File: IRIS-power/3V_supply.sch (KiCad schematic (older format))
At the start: 3 parts

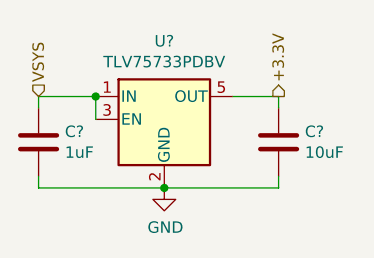
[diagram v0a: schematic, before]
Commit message: Finalized power board V2 schematic, preparing to layout
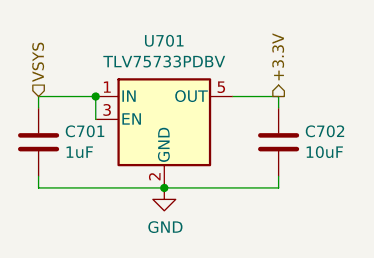
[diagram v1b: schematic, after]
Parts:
- C701, C702: renamed from C?; footprint (none) -> Capacitor_SMD:C_0603_1608Metric
- gave numbers to parts that had none: 1
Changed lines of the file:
@@
 $Descr A4 11693 8268
 encoding utf-8
-Sheet 2 9
+Sheet 7 8
 Title ""
 Date ""
@@
 	5650 3900 5650 3800
 $Comp
-L power:GND #PWR?
+L power:GND #PWR0701
 U 1 1 5F36182F
 P 5950 4200
-F 0 "#PWR?" H 5950 3950 50  0001 C CNN
+F 0 "#PWR0701" H 5950 3950 50  0001 C CNN
 F 1 "GND" H 5955 4027 50  0000 C CNN
 F 2 "" H 5950 4200 50  0001 C CNN
@@
 	6450 3850 6450 3800
 $Comp
-L Device:C C?
+L Device:C C702
 U 1 1 5F36183D
 P 6450 4000
-F 0 "C?" H 6565 4046 50  0000 L CNN
+F 0 "C702" H 6565 4046 50  0000 L CNN
 F 1 "10uF" H 6565 3955 50  0000 L CNN
-F 2 "" H 6488 3850 50  0001 C CNN
+F 2 "Capacitor_SMD:C_0603_1608Metric" H 6488 3850 50  0001 C CNN
 F 3 "~" H 6450 4000 50  0001 C CNN
 	1    6450 4000
@@
 $EndComp
 $Comp
-L Device:C C?
+L Device:C C701
 U 1 1 5F361843
 P 5400 4000
-F 0 "C?" H 5515 4046 50  0000 L CNN
+F 0 "C701" H 5515 4046 50  0000 L CNN
 F 1 "1uF" H 5515 3955 50  0000 L CNN
-F 2 "" H 5438 3850 50  0001 C CNN
+F 2 "Capacitor_SMD:C_0603_1608Metric" H 5438 3850 50  0001 C CNN
 F 3 "~" H 5400 4000 50  0001 C CNN
 	1    5400 4000
@@
 Connection ~ 5650 3800
 $Comp
-L Regulator_Linear:TLV75733PDBV U?
+L Regulator_Linear:TLV75733PDBV U701
 U 1 1 5F36184A
 P 5950 3900
-F 0 "U?" H 5950 4242 50  0000 C CNN
+F 0 "U701" H 5950 4242 50  0000 C CNN
 F 1 "TLV75733PDBV" H 5950 4151 50  0000 C CNN
 F 2 "Package_TO_SOT_SMD:SOT-23-5" H 5950 4225 50  0001 C CIN

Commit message: Finished initial layout without gnd plane
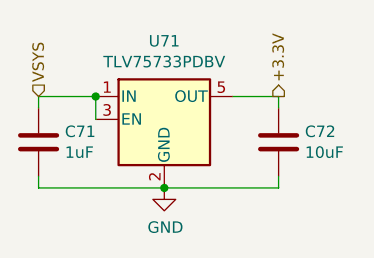
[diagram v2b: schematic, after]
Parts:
- renumbered C701 to C71, C702 to C72, U701 to U71
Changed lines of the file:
@@
 	5650 3900 5650 3800
 $Comp
-L power:GND #PWR0701
+L power:GND #PWR0103
 U 1 1 5F36182F
 P 5950 4200
-F 0 "#PWR0701" H 5950 3950 50  0001 C CNN
+F 0 "#PWR0103" H 5950 3950 50  0001 C CNN
 F 1 "GND" H 5955 4027 50  0000 C CNN
 F 2 "" H 5950 4200 50  0001 C CNN
@@
 	6450 3850 6450 3800
 $Comp
-L Device:C C702
+L Device:C C72
 U 1 1 5F36183D
 P 6450 4000
-F 0 "C702" H 6565 4046 50  0000 L CNN
+F 0 "C72" H 6565 4046 50  0000 L CNN
 F 1 "10uF" H 6565 3955 50  0000 L CNN
 F 2 "Capacitor_SMD:C_0603_1608Metric" H 6488 3850 50  0001 C CNN
@@
 $EndComp
 $Comp
-L Device:C C701
+L Device:C C71
 U 1 1 5F361843
 P 5400 4000
-F 0 "C701" H 5515 4046 50  0000 L CNN
+F 0 "C71" H 5515 4046 50  0000 L CNN
 F 1 "1uF" H 5515 3955 50  0000 L CNN
 F 2 "Capacitor_SMD:C_0603_1608Metric" H 5438 3850 50  0001 C CNN
@@
 Connection ~ 5650 3800
 $Comp
-L Regulator_Linear:TLV75733PDBV U701
+L Regulator_Linear:TLV75733PDBV U71
 U 1 1 5F36184A
 P 5950 3900
-F 0 "U701" H 5950 4242 50  0000 C CNN
+F 0 "U71" H 5950 4242 50  0000 C CNN
 F 1 "TLV75733PDBV" H 5950 4151 50  0000 C CNN
 F 2 "Package_TO_SOT_SMD:SOT-23-5" H 5950 4225 50  0001 C CIN

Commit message: Improved fuel gauge layout
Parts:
- C71: Digikey PN (none) -> 1276-1102-1-ND
- C72: Digikey PN (none) -> 1276-1192-1-ND
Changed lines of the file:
@@
 F 2 "Capacitor_SMD:C_0603_1608Metric" H 6488 3850 50  0001 C CNN
 F 3 "~" H 6450 4000 50  0001 C CNN
+F 4 "1276-1192-1-ND" H 6450 4000 50  0001 C CNN "Digikey PN"
 	1    6450 4000
 	1    0    0    -1
@@
 F 2 "Capacitor_SMD:C_0603_1608Metric" H 5438 3850 50  0001 C CNN
 F 3 "~" H 5400 4000 50  0001 C CNN
+F 4 "1276-1102-1-ND" H 5400 4000 50  0001 C CNN "Digikey PN"
 	1    5400 4000
 	1    0    0    -1

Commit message: Adjusted silkscreen
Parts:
- U71: Digikey PN (none) -> 296-50414-1-ND
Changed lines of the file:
@@
 F 2 "Package_TO_SOT_SMD:SOT-23-5" H 5950 4225 50  0001 C CIN
 F 3 "https://www.ti.com/lit/ds/symlink/tlv757p.pdf" H 5950 3950 50  0001 C CNN
+F 4 "296-50414-1-ND" H 5950 3900 50  0001 C CNN "Digikey PN"
 	1    5950 3900
 	1    0    0    -1

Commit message: Updated to V4.01
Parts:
- C71: Digikey PN 1276-1102-1-ND -> 1276-1860-1-ND
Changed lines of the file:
@@
 F 2 "Capacitor_SMD:C_0603_1608Metric" H 5438 3850 50  0001 C CNN
 F 3 "~" H 5400 4000 50  0001 C CNN
-F 4 "1276-1102-1-ND" H 5400 4000 50  0001 C CNN "Digikey PN"
+F 4 "1276-1860-1-ND" H 5400 4000 50  0001 C CNN "Digikey PN"
 	1    5400 4000
 	1    0    0    -1
